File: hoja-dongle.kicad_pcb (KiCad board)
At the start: 2 copper layers, 30 x 44 mm, 64 parts, among them J2 USB4080-03-A_REVA1, J3 Conn_01x04_Pin, P1 RPI-RM2, Q1 BSS138DW, Q2 BSS138DW, SW1 1TS026A-1000-0550, SW2 SW_Push, SW3 SW_Push, U1 USBLC6-2P6, U2 USBLC6-2P6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

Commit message: prod
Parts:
- added R13: 51K, Resistor_SMD:R_0201_0603Metric, F.Cu at (119.7, 39.7)
- R19, R20, R21: value 100R -> 27R
- moved Y1 0.99 mm to (103.2, 44.8)
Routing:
- net +3V3_PRE: track 31.2 -> 32.7 mm
- net XTAL_IN: track 9.67 -> 8.67 mm
- net Net-(C2-Pad1): track 4.53 -> 3.55 mm

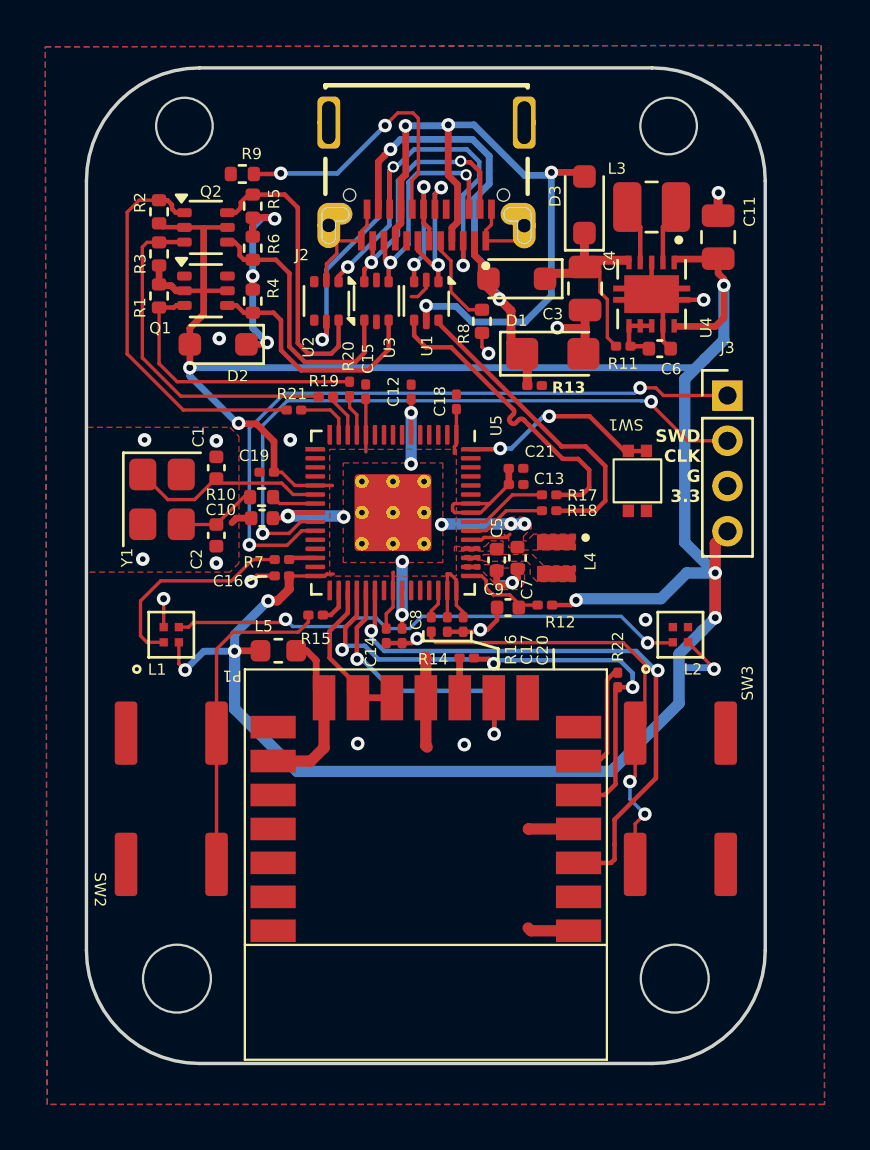
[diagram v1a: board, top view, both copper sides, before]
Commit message: resolve missing trace
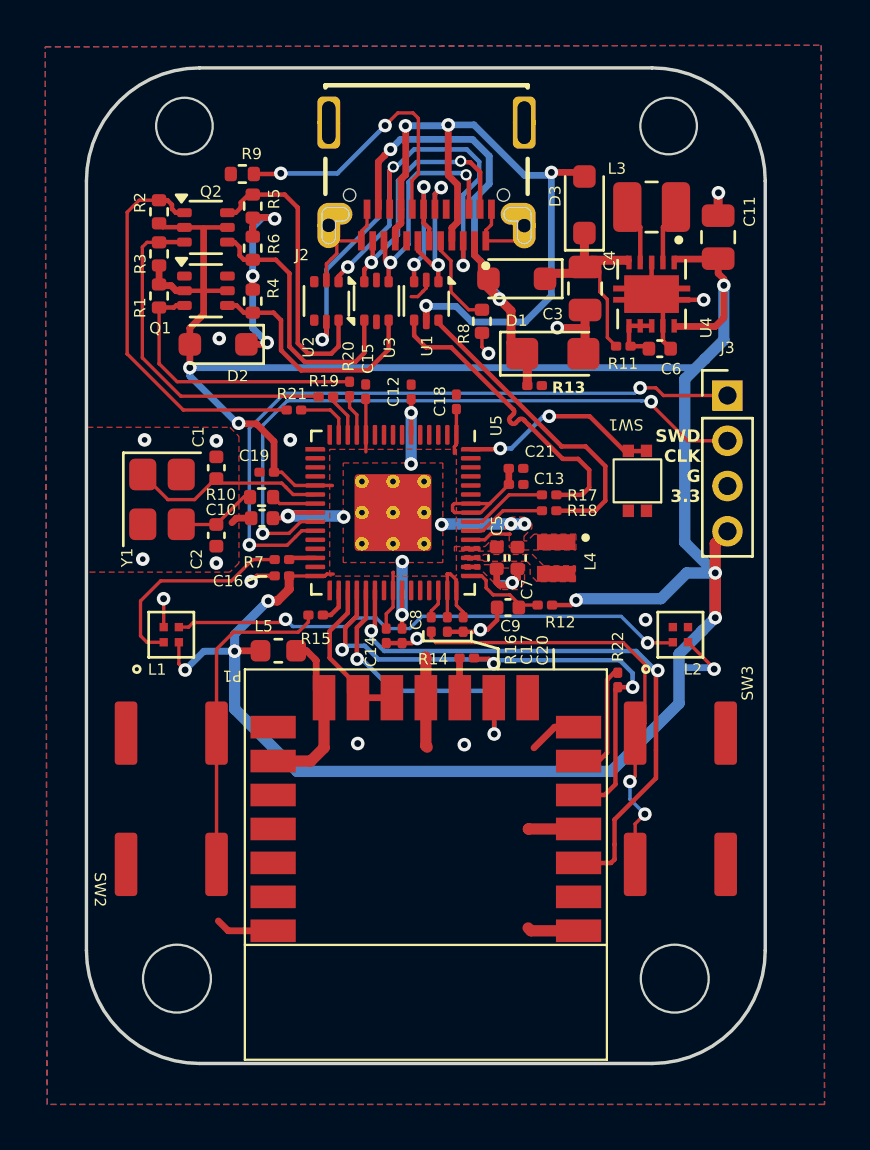
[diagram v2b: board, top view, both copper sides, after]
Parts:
- moved C5 0.09 mm to (118.0, 47.4)
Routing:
- net GND: track 39.4 -> 44.3 mm
